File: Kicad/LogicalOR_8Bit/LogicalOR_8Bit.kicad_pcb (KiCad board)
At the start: 2 copper layers, 39.3 x 66.3 mm, 65 parts, among them J1 Conn_01x26_Pin, Q1 NPN, Q10 NPN, Q11 NPN, Q12 NPN, Q13 NPN, Q14 NPN, Q15 NPN, Q16 NPN, Q17 NPN, Q18 NPN, Q19 NPN, Q2 NPN, Q20 NPN, Q21 NPN, Q22 NPN, Q23 NPN, Q24 NPN, Q3 NPN, Q4 NPN, Q5 NPN, Q6 NPN, Q7 NPN, Q8 NPN, Q9 NPN

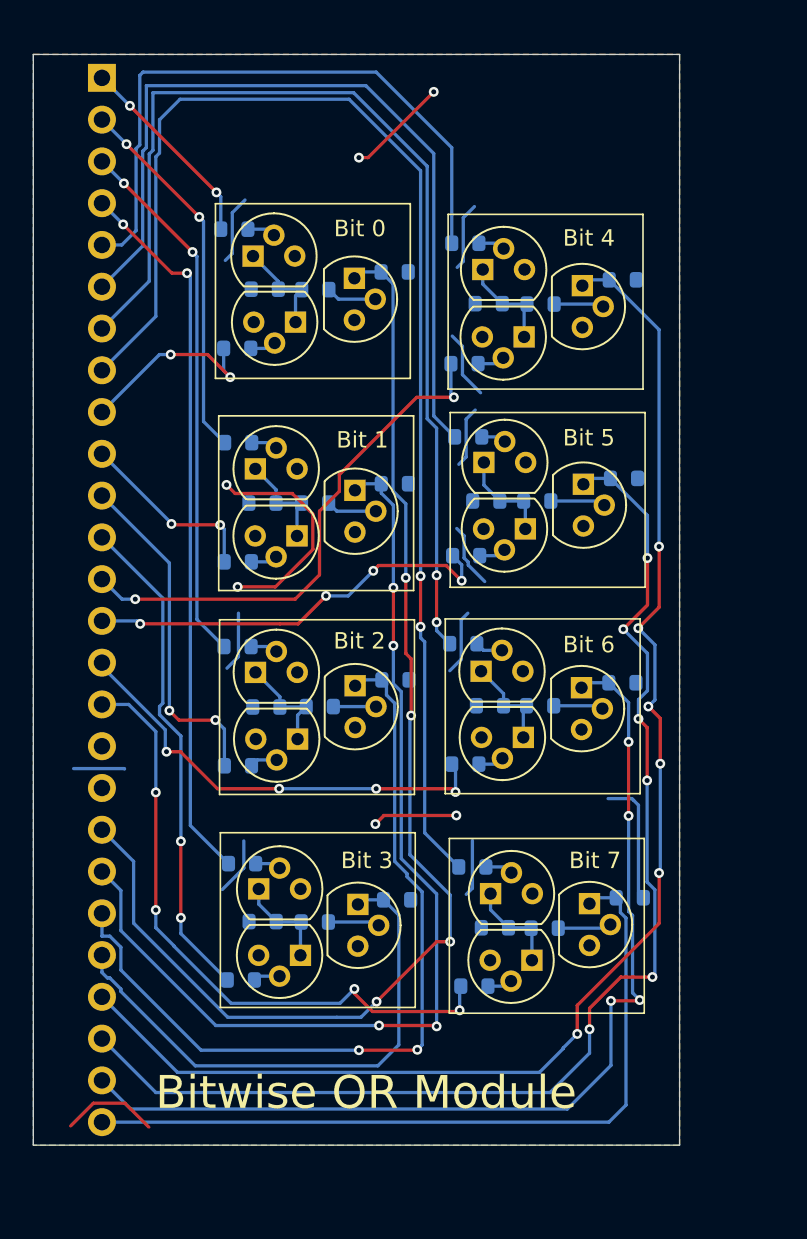
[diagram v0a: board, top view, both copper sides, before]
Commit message: Finished the XOR module and added silk screens to OR, AND, and XOR
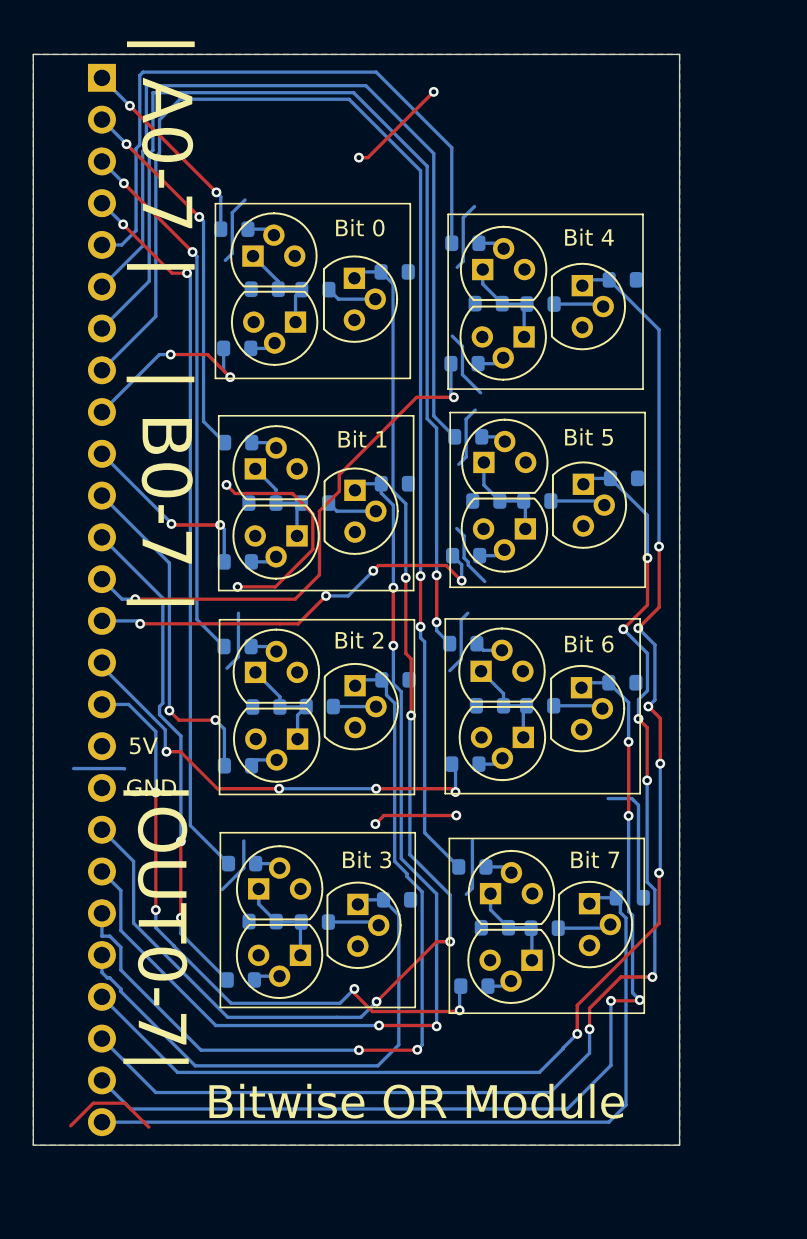
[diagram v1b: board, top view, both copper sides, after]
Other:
- board text added: "5V"
- board text added: "GND"
- board text added: "| A0-7 |"
- board text added: "| B0-7 |"
- board text added: "|OUT0-7|"
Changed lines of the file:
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@@
 		(layer "Edge.Cuts")
+	)
+	(gr_text "GND"
+		(at 51.37 142.71 0)
+		(layer "F.SilkS")
+		(effects
+			(font
+				(size 1 1)
+				(thickness 0.15)
+			)
+			(justify left bottom)
+		)
 	)
 	(gr_text "Bit 5"
@@
 		)
 	)
+	(gr_text "| A0-7 |"
+		(at 52.05 96.19 -90)
+		(layer "F.SilkS")
+		(effects
+			(font
+				(size 3 3)
+				(thickness 0.45)
+			)
+			(justify left bottom)
+		)
+	)
+	(gr_text "| B0-7 |"
+		(at 52.03 116.57 -90)
+		(layer "F.SilkS")
+		(effects
+			(font
+				(size 3 3)
+				(thickness 0.45)
+			)
+			(justify left bottom)
+		)
+	)
 	(gr_text "Bit 7"
 		(at 78.325 147.1 0)
@@
 	)
 	(gr_text "Bitwise OR Module"
-		(at 53.175 161.8 0)
+		(at 56.19 162.42 0)
 		(layer "F.SilkS")
 		(effects
@@
 		(layer "F.SilkS")
 		(effects
+			(font
+				(size 1 1)
+				(thickness 0.15)
+			)
+			(justify left bottom)
+		)
+	)
+	(gr_text "|OUT0-7|"
+		(at 51.81 141.74 -90)
+		(layer "F.SilkS")
+		(effects
+			(font
+				(size 2.9 2.9)
+				(thickness 0.435)
+			)
+			(justify left bottom)
+		)
+	)
+	(gr_text "5V"
+		(at 51.52 140.16 0)
+		(layer "F.SilkS")
+		(effects
